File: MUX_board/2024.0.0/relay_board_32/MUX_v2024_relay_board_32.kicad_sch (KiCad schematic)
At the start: 23 parts, among them J1 Relays Pwr, J2 I2C, J3 Screw_Terminal_01x04, J4 Conn_02x08_Odd_Even, J5 Screw_Terminal_01x16, U1 MCP23017_SP, U2 MCP23017_SP

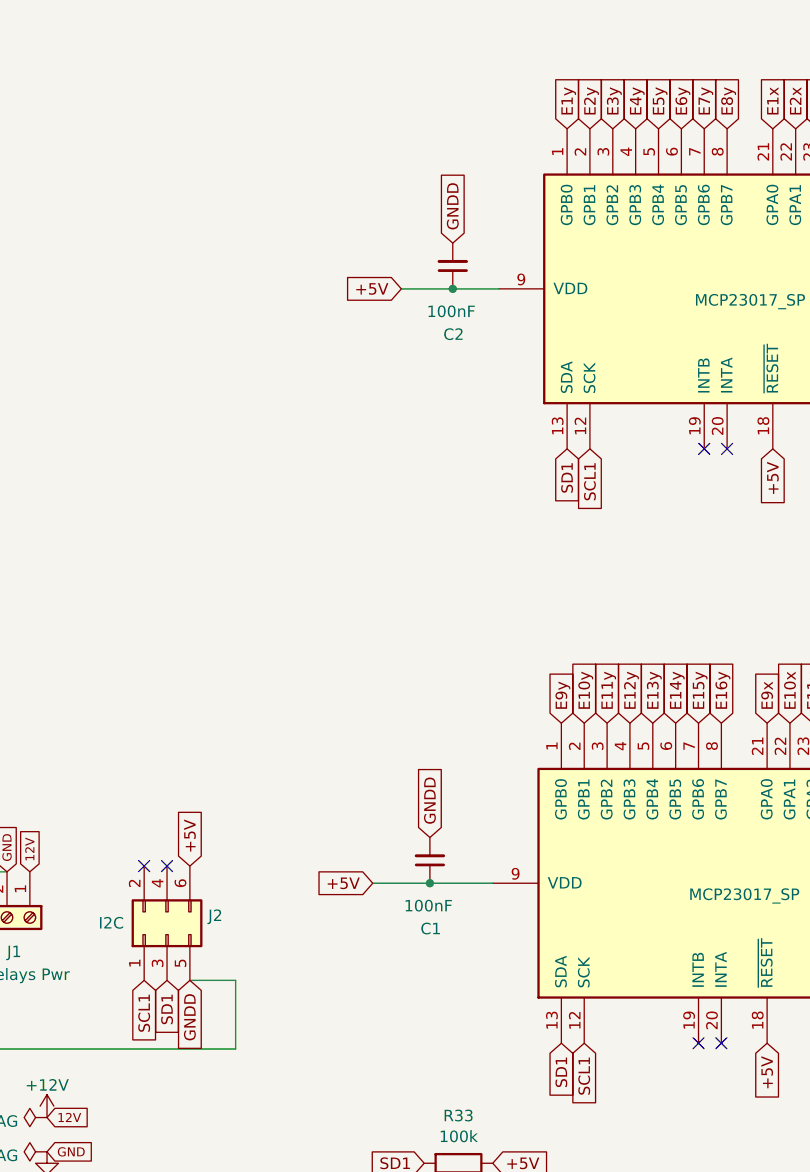
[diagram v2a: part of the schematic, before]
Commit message: adds filtering capacitors on MCP23017
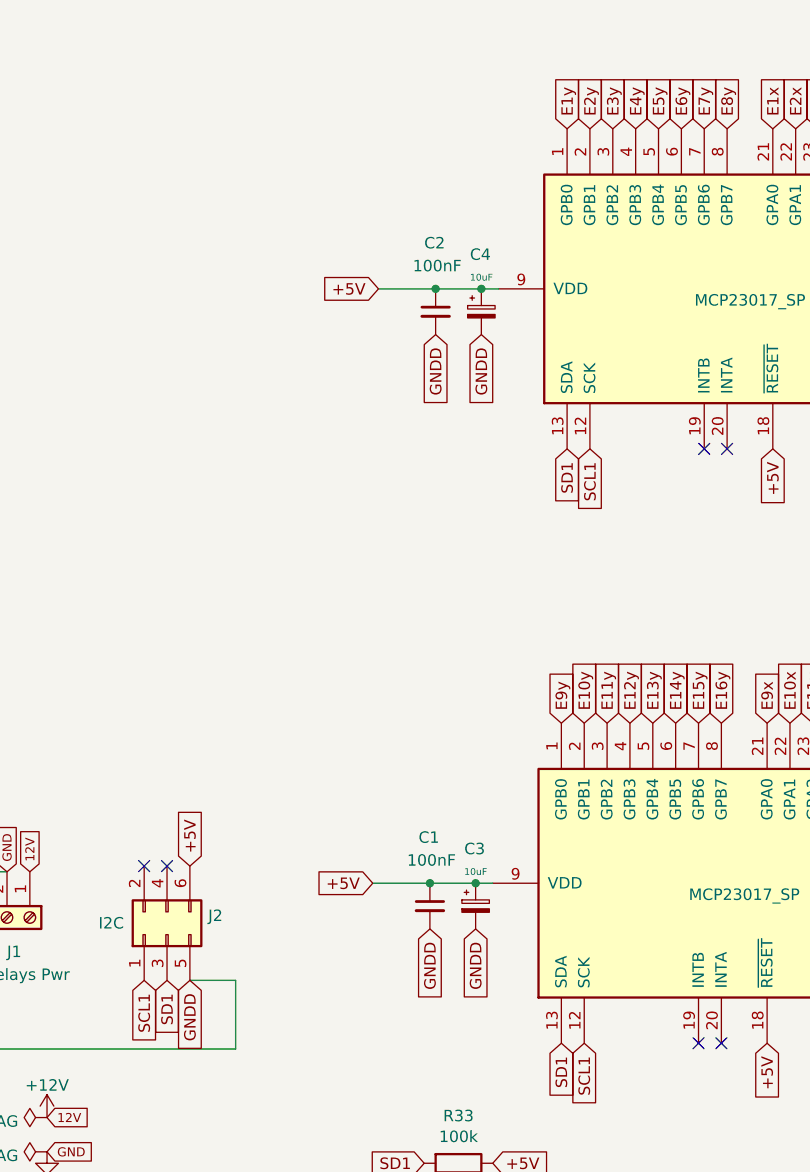
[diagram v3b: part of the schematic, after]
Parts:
- added C3, C4: 10uF, Capacitor_THT:CP_Radial_D6.3mm_P2.50mm, symbol Device:C_Polarized_Small
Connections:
- net +5V: now also C3.1, C4.1
- net GND: now also C3.2, C4.2
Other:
- moved on the sheet: C1
